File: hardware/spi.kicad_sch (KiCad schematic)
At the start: 3 parts, among them J2 DeadOn RTC

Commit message: Added Board Register
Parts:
- removed D1: LED, symbol Device:LED
- removed R16: 330, Resistor_SMD:R_0603_1608Metric, symbol Device:R_Small_US
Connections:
- net +5V is gone; now on net +3.3V: J2.2 (VCC)
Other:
- title: (none) -> Lambda One - Internal SPI

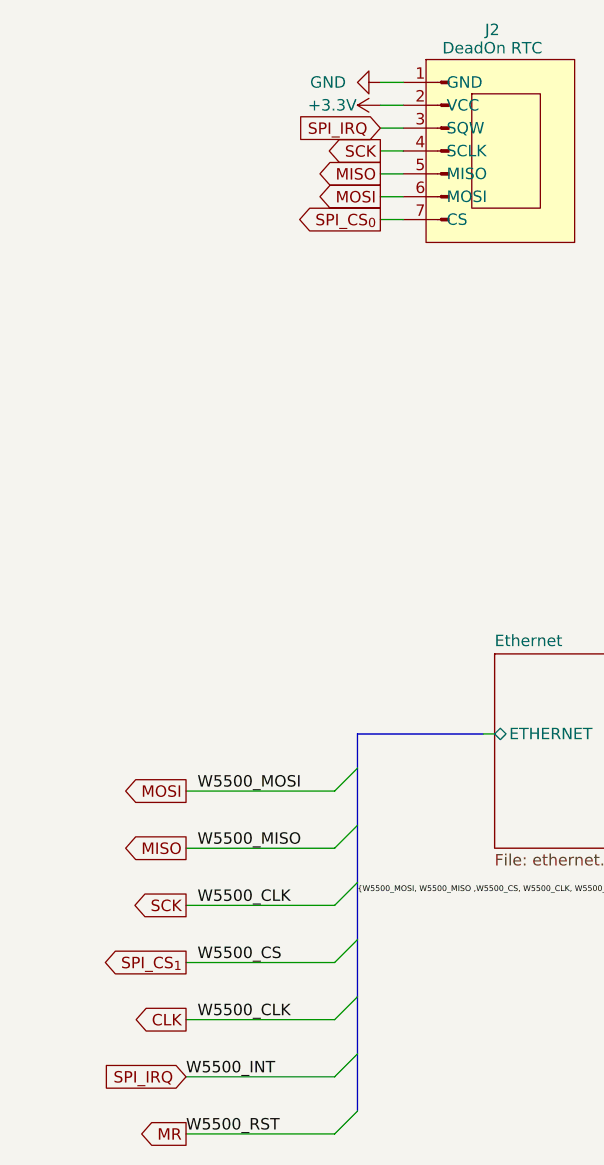
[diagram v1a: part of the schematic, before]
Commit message: Added External connectors
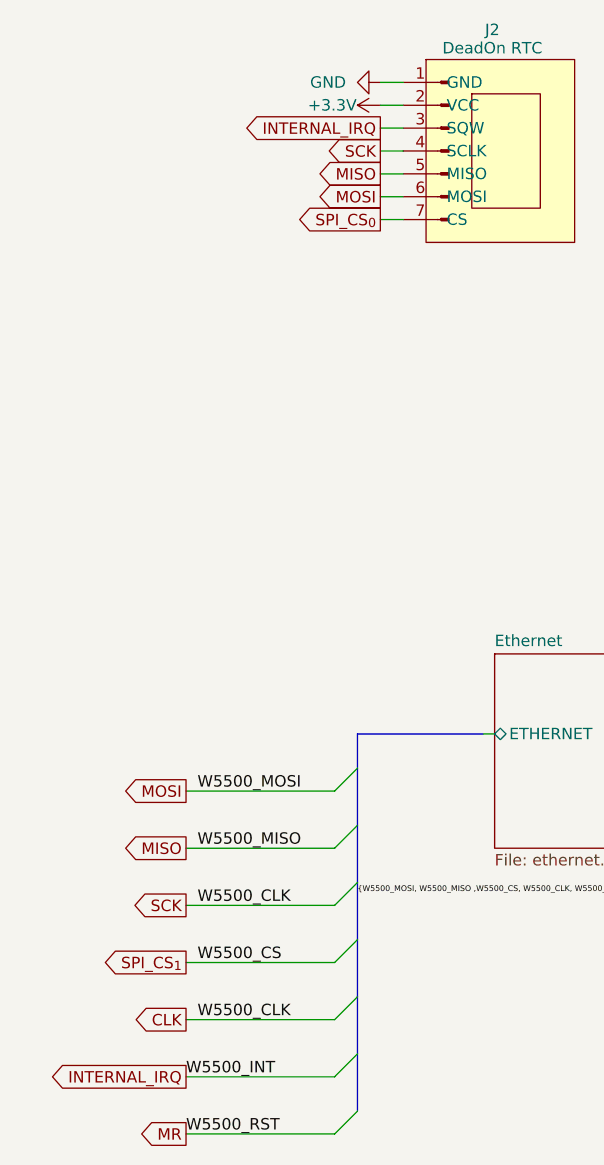
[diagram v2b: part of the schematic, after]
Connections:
- net SPI_IRQ renamed INTERNAL_IRQ
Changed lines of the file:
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@@
+		)
+	)
+	(global_label "INTERNAL_IRQ"
+		(shape output)
+		(at 57.15 154.94 180)
+		(fields_autoplaced yes)
+		(effects
+			(font
+				(size 1.27 1.27)
+			)
+			(justify right)
+		)
+		(property "Intersheetrefs" "${INTERSHEET_REFS}"
+			(at 41.2228 154.94 0)
+			(effects
+				(font
+					(size 1.27 1.27)
+				)
+				(justify right)
+				(hide yes)
+			)
 		)
 	)
@@
 		(property "Intersheetrefs" "${INTERSHEET_REFS}"
 			(at 72.0053 52.07 0)
-			(effects
-				(font
-					(size 1.27 1.27)
-				)
-				(justify right)
-				(hide yes)
-			)
-		)
-	)
-	(global_label "SPI_IRQ"
-		(shape input)
-		(at 78.74 49.53 180)
-		(fields_autoplaced yes)
-		(effects
-			(font
-				(size 1.27 1.27)
-			)
-			(justify right)
-		)
-		(property "Intersheetrefs" "${INTERSHEET_REFS}"
-			(at 68.4976 49.53 0)
 			(effects
 				(font
@@
 		)
 	)
-	(global_label "SPI_IRQ"
-		(shape input)
-		(at 57.15 154.94 180)
-		(fields_autoplaced yes)
-		(effects
-			(font
-				(size 1.27 1.27)
-			)
-			(justify right)
-		)
-		(property "Intersheetrefs" "${INTERSHEET_REFS}"
-			(at 46.9076 154.94 0)
-			(effects
-				(font
-					(size 1.27 1.27)
-				)
-				(justify right)
-				(hide yes)
-			)
-		)
-	)
 	(global_label "MOSI"
 		(shape output)
@@
 			(effects
 				(font
+					(size 1.27 1.27)
+				)
+				(justify right)
+				(hide yes)
+			)
+		)
+	)
+	(global_label "INTERNAL_IRQ"
+		(shape output)
+		(at 78.74 49.53 180)
+		(fields_autoplaced yes)
+		(effects
+			(font
+				(size 1.27 1.27)
+			)
+			(justify right)
+		)
+		(property "Intersheetrefs" "${INTERSHEET_REFS}"
+			(at 62.8128 49.53 0)
+			(effects
+				(font

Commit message: Fixed some erros, changed to 3V
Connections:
- net CLK renamed SCK
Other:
- sheet Ethernet ports: added none; removed ETHERNET

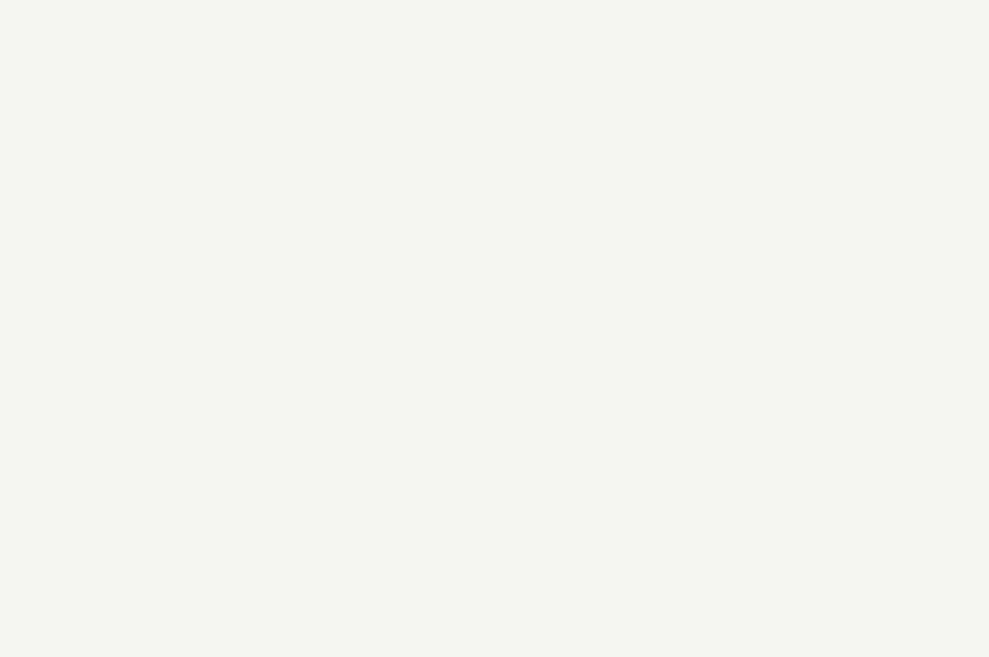
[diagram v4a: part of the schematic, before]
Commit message: Fixed critical bugs on the system related to memory maping and IC selections
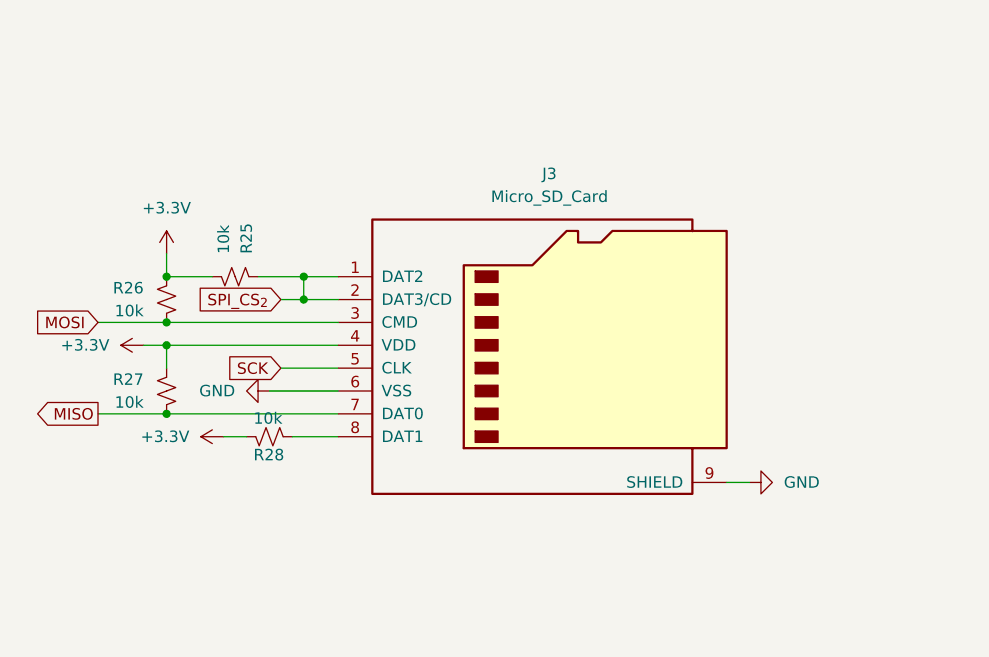
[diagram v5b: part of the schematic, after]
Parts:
- added J3: Micro_SD_Card, symbol Connector:Micro_SD_Card
- added R25, R26, R27, R28: 10k, Resistor_SMD:R_0603_1608Metric, symbol Device:R_Small_US
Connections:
- net +3.3V: now also J3.4 (VDD), R25.2, R26.1, R27.1, R28.2
- net GND: now also J3.6 (VSS), J3.9 (SHIELD)
- net MISO: now also J3.7 (DAT0), R27.2
- net MOSI: now also J3.3 (CMD), R26.2
- net SCK: now also J3.5 (CLK)
- new net: J3.8 (DAT1), R28.1
- new net SPI_CS_{2}: J3.1 (DAT2), J3.2 (DAT3/CD), R25.1

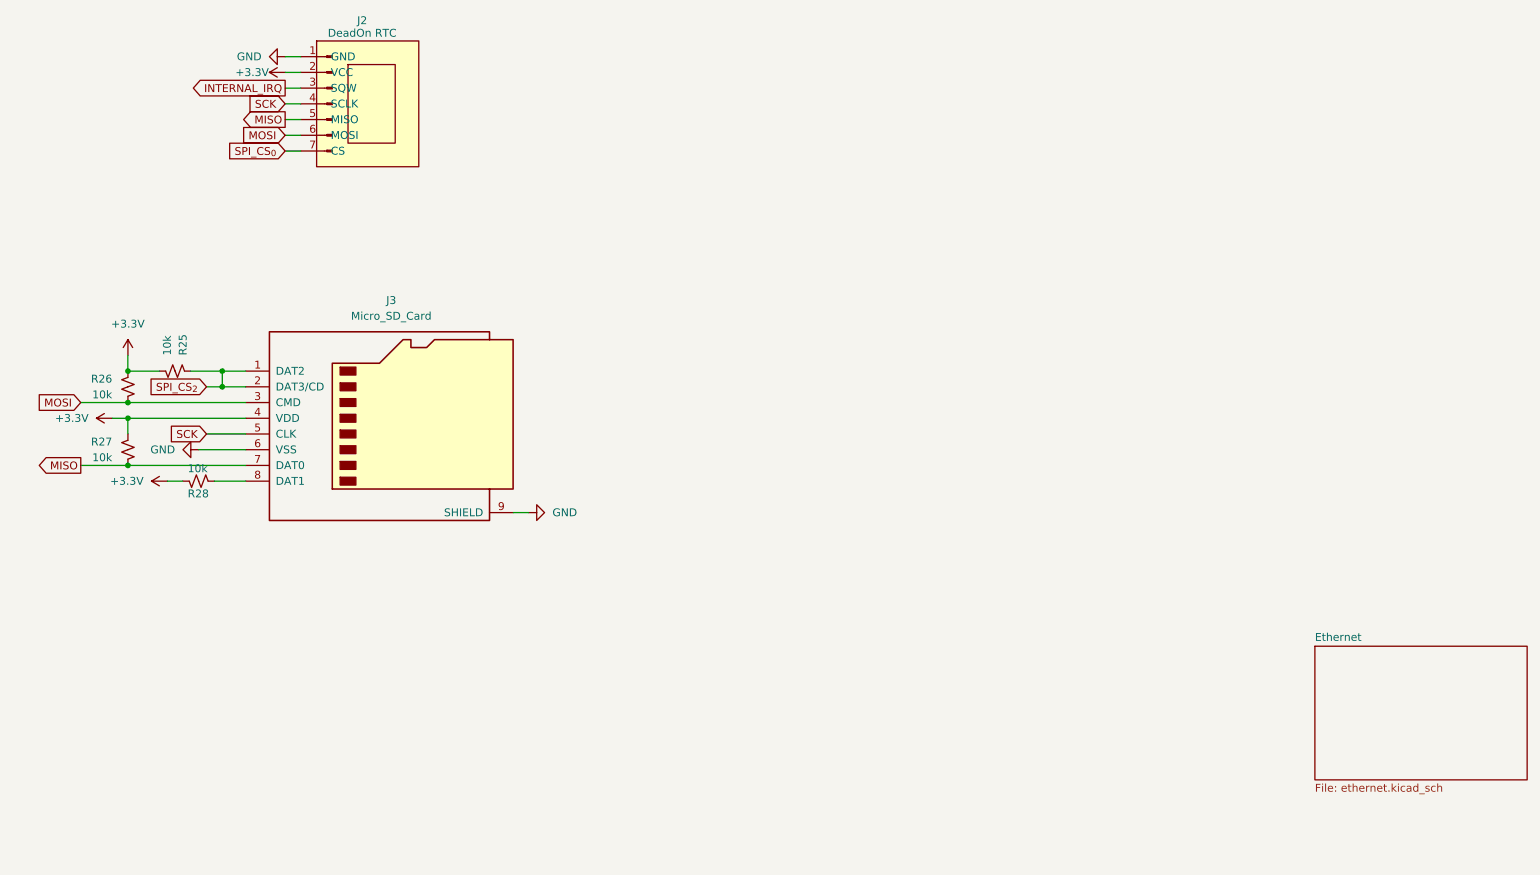
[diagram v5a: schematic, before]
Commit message: Changed Ethernet Chip to Ethernet ModuleWIZ850IO
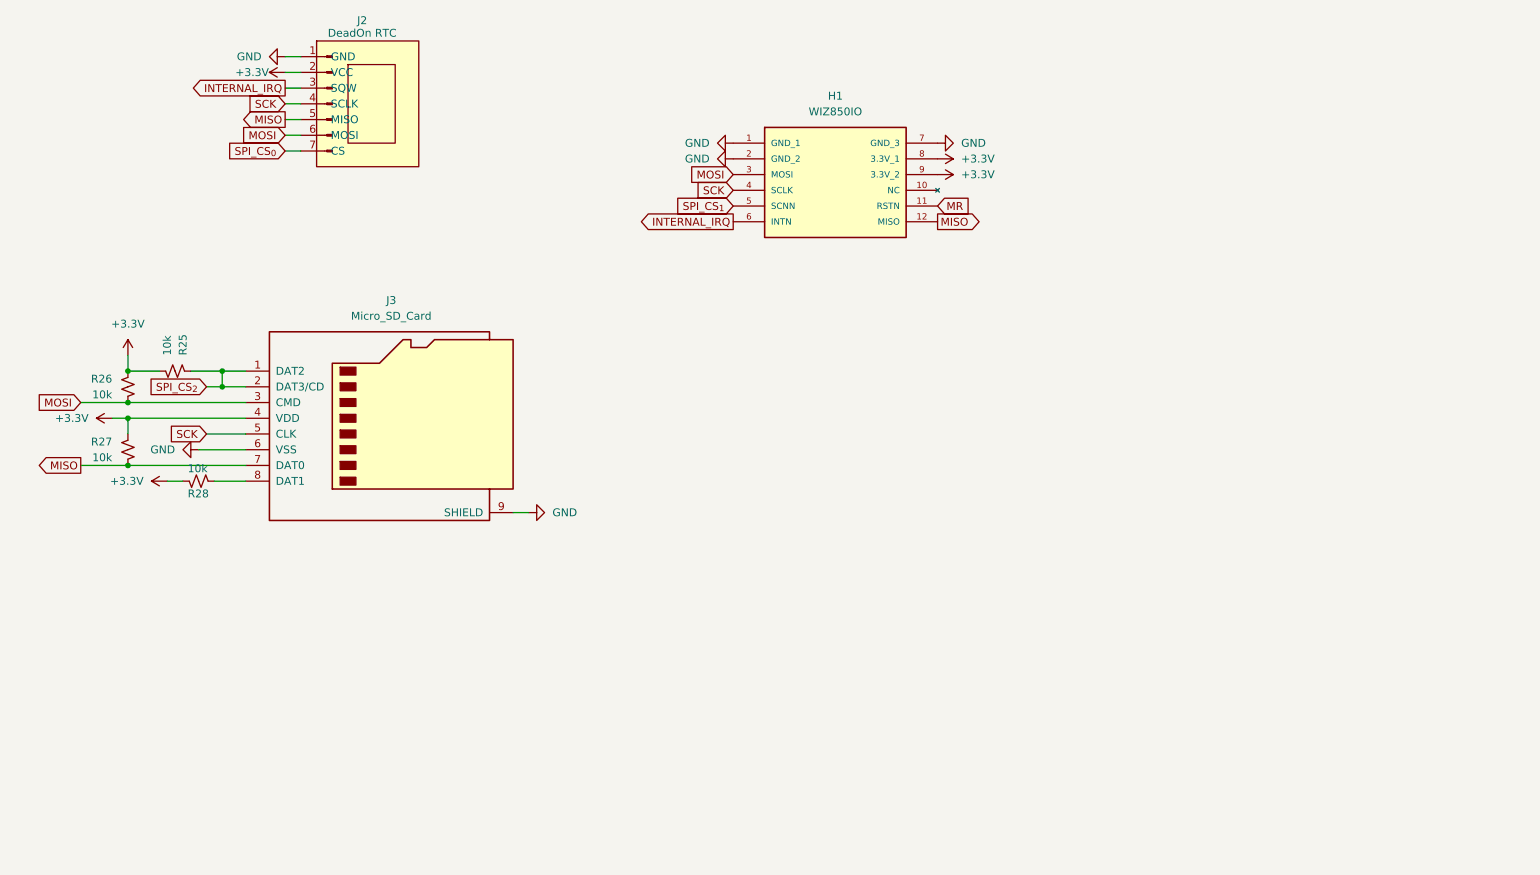
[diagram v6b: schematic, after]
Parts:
- added H1: WIZ850IO, AT28C256-15PU:WIZ850IO, symbol net:WIZ850IO
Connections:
- net +3.3V: now also H1.8 (3.3V_1), H1.9 (3.3V_2)
- net GND: now also H1.1 (GND_1), H1.2 (GND_2), H1.7 (GND_3)
- net INTERNAL_IRQ: now also H1.6 (INTN)
- net MISO: now also H1.12 (MISO)
- net MOSI: now also H1.3 (MOSI)
- net SCK: now also H1.4 (SCLK)
- new net MR: H1.11 (RSTN)
- new net SPI_CS_{1}: H1.5 (SCNN)
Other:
- removed sheet Ethernet

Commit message: Fixes and addres fix adding VDA AND VPA
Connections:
- net +3.3V: now also R25.1, R28.1; no longer R25.2, R28.2
- net SPI_CS_{2}: now also R25.2; no longer R25.1
- net at J3.8 (DAT1): now also R28.2; no longer R28.1
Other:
- moved on the sheet: H1, J2, J3, R25, R26, R27, R28
